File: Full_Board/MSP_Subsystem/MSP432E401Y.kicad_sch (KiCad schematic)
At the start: 4 parts, among them J1-J3 Conn_01x10, J4-J2 Conn_01x10, J5-J7 Conn_01x10, J8-J6 Conn_01x10

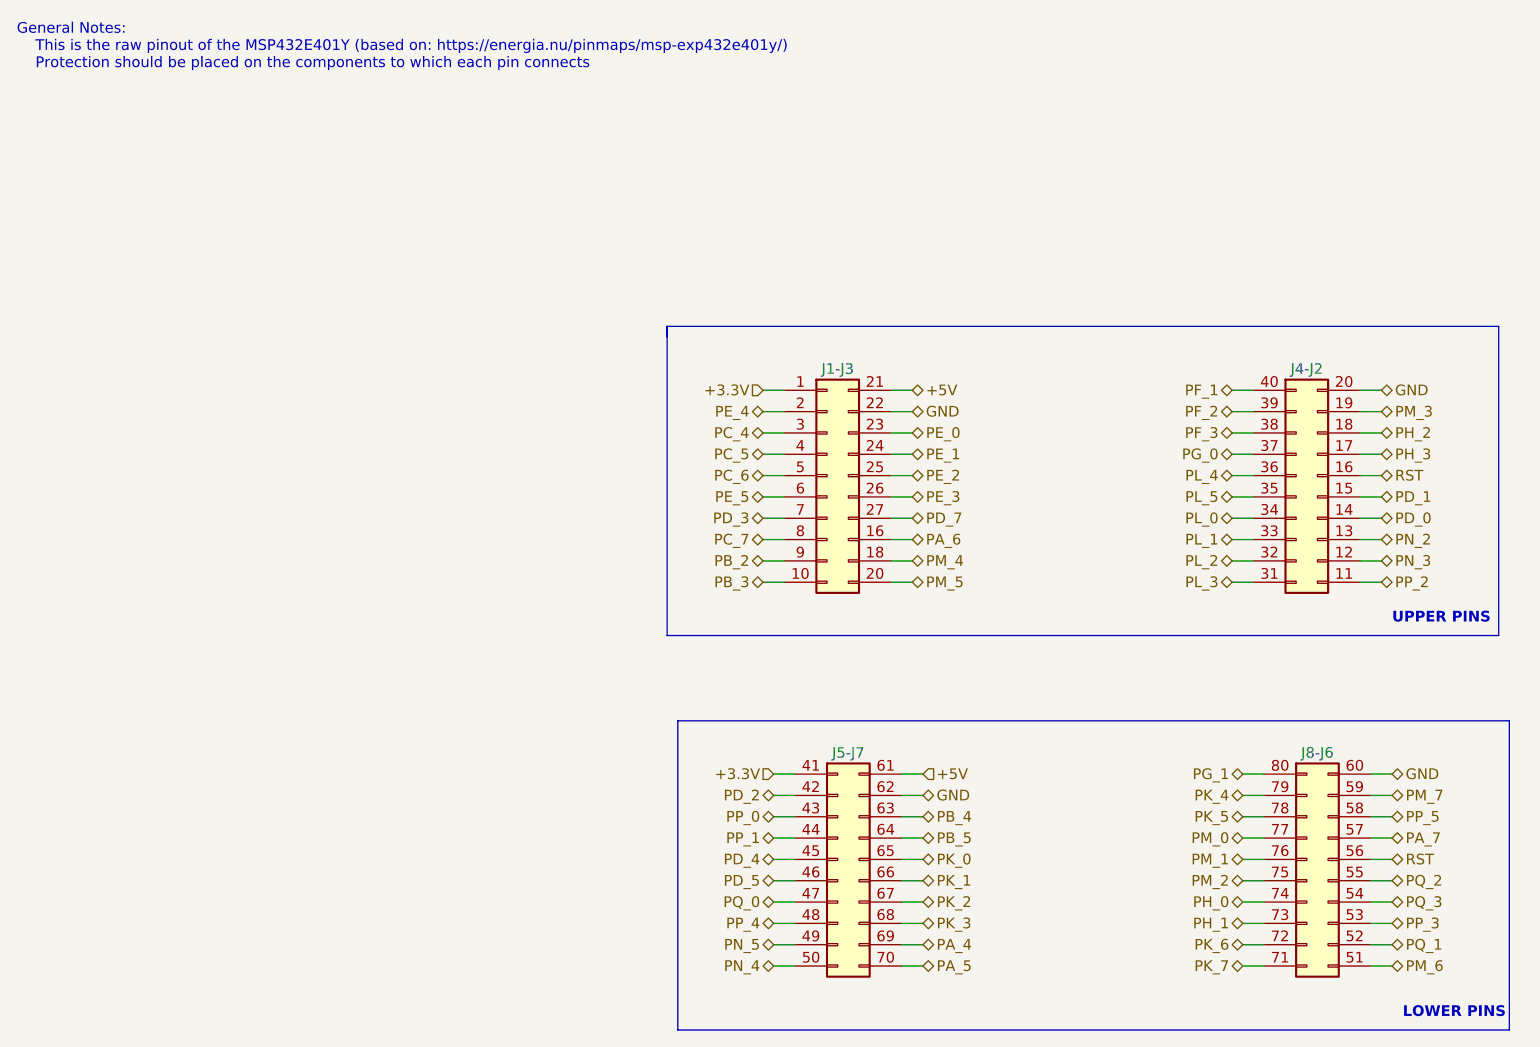
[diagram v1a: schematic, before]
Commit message: Add digikey/mouser components to stepper and button subsystems
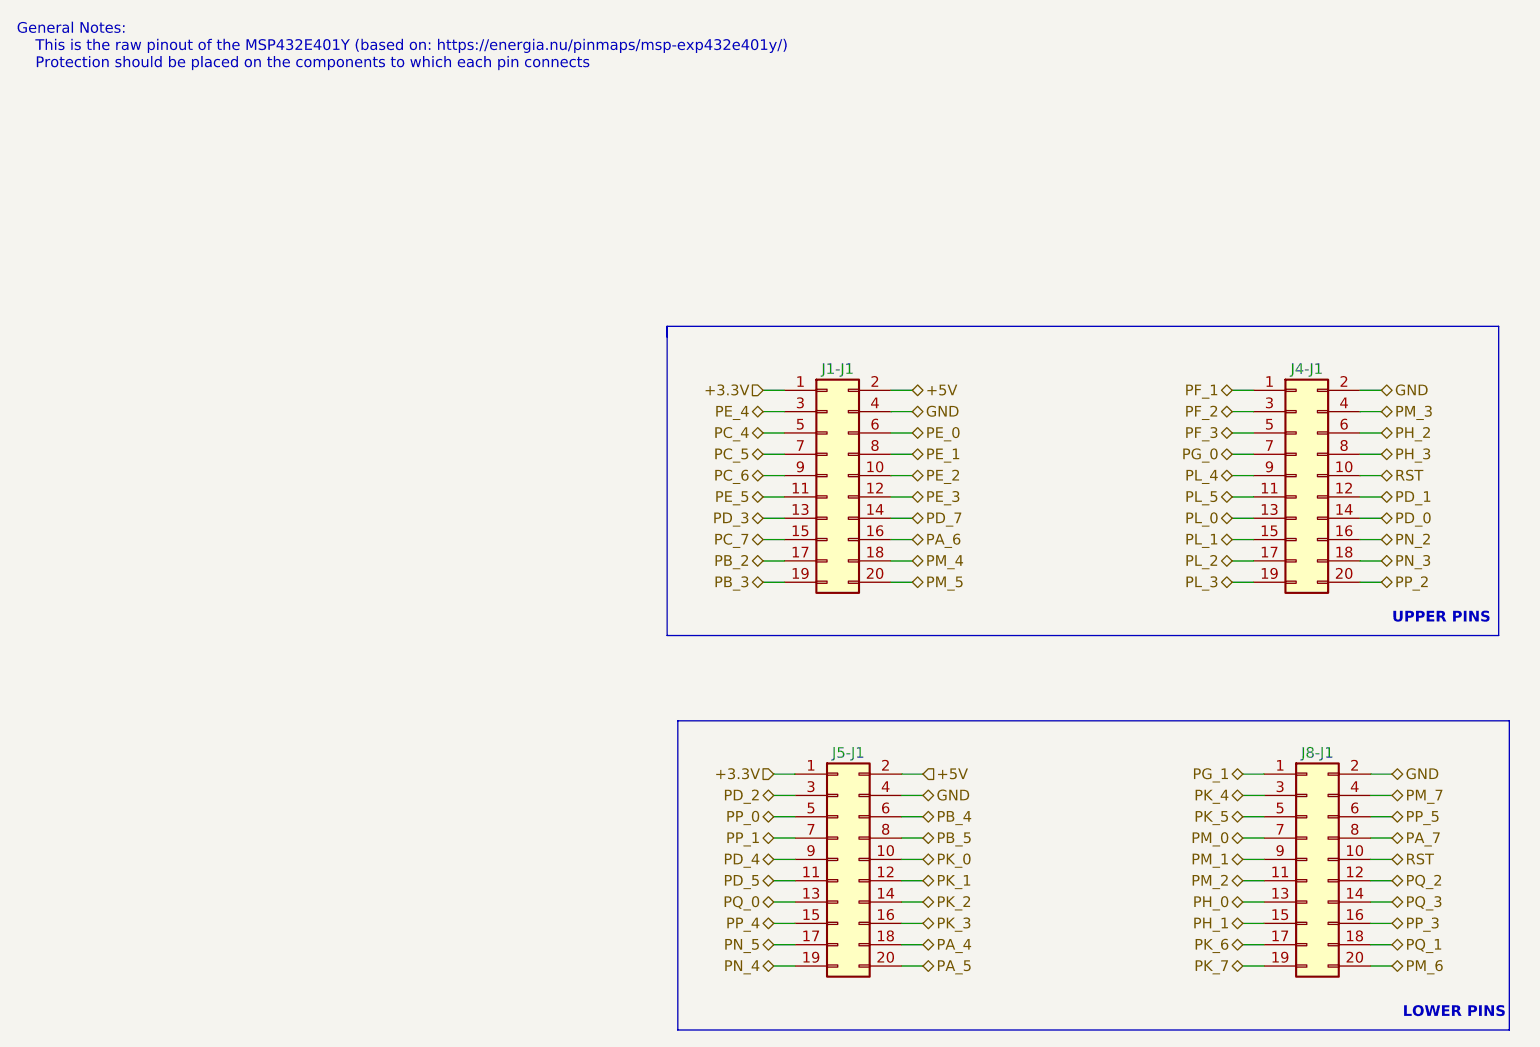
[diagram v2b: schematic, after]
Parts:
- renumbered J1-J3 to J1-J1, J4-J2 to J4-J1, J5-J7 to J5-J1, J8-J6 to J8-J1
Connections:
- net +3.3V: now also J5-J1.1 (Pin_1); no longer J5-J1.41 (Pin_41)
- net +5V: now also J1-J1.2 (Pin_2), J5-J1.2 (Pin_2); no longer J1-J1.21 (Pin_21), J5-J1.61 (Pin_61)
- net GND: now also J1-J1.4 (Pin_4), J4-J1.2 (Pin_2), J5-J1.4 (Pin_4), J8-J1.2 (Pin_2); no longer J1-J1.22 (Pin_22), J4-J1.20 (Pin_20), J5-J1.62 (Pin_62), J8-J1.60 (Pin_60)
- net PA_4: now also J5-J1.18 (Pin_18); no longer J5-J1.69 (Pin_69)
- net PA_5: now also J5-J1.20 (Pin_20); no longer J5-J1.70 (Pin_70)
- net PA_7: now also J8-J1.8 (Pin_8); no longer J8-J1.57 (Pin_57)
- net PB_2: now also J1-J1.17 (Pin_17); no longer J1-J1.9 (Pin_9)
- net PB_3: now also J1-J1.19 (Pin_19); no longer J1-J1.10 (Pin_10)
- net PB_4: now also J5-J1.6 (Pin_6); no longer J5-J1.63 (Pin_63)
- net PB_5: now also J5-J1.8 (Pin_8); no longer J5-J1.64 (Pin_64)
- net PC_4: now also J1-J1.5 (Pin_5); no longer J1-J1.3 (Pin_3)
- net PC_5: now also J1-J1.7 (Pin_7); no longer J1-J1.4
- net PC_6: now also J1-J1.9 (Pin_9); no longer J1-J1.5 (Pin_5)
- net PC_7: now also J1-J1.15 (Pin_15); no longer J1-J1.8 (Pin_8)
- net PD_1: now also J4-J1.12 (Pin_12); no longer J4-J1.15 (Pin_15)
- net PD_2: now also J5-J1.3 (Pin_3); no longer J5-J1.42 (Pin_42)
- net PD_3: now also J1-J1.13 (Pin_13); no longer J1-J1.7 (Pin_7)
- net PD_4: now also J5-J1.9 (Pin_9); no longer J5-J1.45 (Pin_45)
- net PD_5: now also J5-J1.11 (Pin_11); no longer J5-J1.46 (Pin_46)
- net PD_7: now also J1-J1.14 (Pin_14); no longer J1-J1.27 (Pin_27)
- net PE_0: now also J1-J1.6 (Pin_6); no longer J1-J1.23 (Pin_23)
- net PE_1: now also J1-J1.8 (Pin_8); no longer J1-J1.24 (Pin_24)
- net PE_2: now also J1-J1.10 (Pin_10); no longer J1-J1.25 (Pin_25)
- net PE_3: now also J1-J1.12 (Pin_12); no longer J1-J1.26 (Pin_26)
- net PE_4: now also J1-J1.3 (Pin_3); no longer J1-J1.2 (Pin_2)
- net PE_5: now also J1-J1.11 (Pin_11); no longer J1-J1.6 (Pin_6)
- net PF_1: now also J4-J1.1 (Pin_1); no longer J4-J1.40 (Pin_40)
- net PF_2: now also J4-J1.3 (Pin_3); no longer J4-J1.39 (Pin_39)
- net PF_3: now also J4-J1.5 (Pin_5); no longer J4-J1.38 (Pin_38)
- net PG_0: now also J4-J1.7 (Pin_7); no longer J4-J1.37 (Pin_37)
- net PG_1: now also J8-J1.1 (Pin_1); no longer J8-J1.80 (Pin_80)
- net PH_0: now also J8-J1.13 (Pin_13); no longer J8-J1.74 (Pin_74)
- net PH_1: now also J8-J1.15 (Pin_15); no longer J8-J1.73 (Pin_73)
- net PH_2: now also J4-J1.6 (Pin_6); no longer J4-J1.18 (Pin_18)
- net PH_3: now also J4-J1.8 (Pin_8); no longer J4-J1.17 (Pin_17)
- net PK_0: now also J5-J1.10 (Pin_10); no longer J5-J1.65 (Pin_65)
- net PK_1: now also J5-J1.12 (Pin_12); no longer J5-J1.66 (Pin_66)
- net PK_2: now also J5-J1.14 (Pin_14); no longer J5-J1.67 (Pin_67)
- net PK_3: now also J5-J1.16 (Pin_16); no longer J5-J1.68 (Pin_68)
- net PK_4: now also J8-J1.3 (Pin_3); no longer J8-J1.79 (Pin_79)
- net PK_5: now also J8-J1.5 (Pin_5); no longer J8-J1.78 (Pin_78)
- net PK_6: now also J8-J1.17 (Pin_17); no longer J8-J1.72 (Pin_72)
- net PK_7: now also J8-J1.19 (Pin_19); no longer J8-J1.71 (Pin_71)
- net PL_0: now also J4-J1.13 (Pin_13); no longer J4-J1.34 (Pin_34)
- net PL_1: now also J4-J1.15 (Pin_15); no longer J4-J1.33 (Pin_33)
- net PL_2: now also J4-J1.17 (Pin_17); no longer J4-J1.32 (Pin_32)
- net PL_3: now also J4-J1.19 (Pin_19); no longer J4-J1.31 (Pin_31)
- net PL_4: now also J4-J1.9 (Pin_9); no longer J4-J1.36 (Pin_36)
- net PL_5: now also J4-J1.11 (Pin_11); no longer J4-J1.35 (Pin_35)
- net PM_0: now also J8-J1.7 (Pin_7); no longer J8-J1.77 (Pin_77)
- net PM_1: now also J8-J1.9 (Pin_9); no longer J8-J1.76 (Pin_76)
- net PM_2: now also J8-J1.11 (Pin_11); no longer J8-J1.75 (Pin_75)
- net PM_3: now also J4-J1.4 (Pin_4); no longer J4-J1.19 (Pin_19)
- net PM_6: now also J8-J1.20 (Pin_20); no longer J8-J1.51 (Pin_51)
- net PM_7: now also J8-J1.4 (Pin_4); no longer J8-J1.59 (Pin_59)
- net PN_2: now also J4-J1.16 (Pin_16); no longer J4-J1.13 (Pin_13)
- net PN_3: now also J4-J1.18 (Pin_18); no longer J4-J1.12 (Pin_12)
- net PN_4: now also J5-J1.19 (Pin_19); no longer J5-J1.50 (Pin_50)
- net PN_5: now also J5-J1.17 (Pin_17); no longer J5-J1.49 (Pin_49)
- net PP_0: now also J5-J1.5 (Pin_5); no longer J5-J1.43 (Pin_43)
- net PP_1: now also J5-J1.7 (Pin_7); no longer J5-J1.44 (Pin_44)
- net PP_2: now also J4-J1.20 (Pin_20); no longer J4-J1.11 (Pin_11)
- net PP_3: now also J8-J1.16 (Pin_16); no longer J8-J1.53 (Pin_53)
- net PP_4: now also J5-J1.15 (Pin_15); no longer J5-J1.48 (Pin_48)
- net PP_5: now also J8-J1.6 (Pin_6); no longer J8-J1.58 (Pin_58)
- net PQ_0: now also J5-J1.13 (Pin_13); no longer J5-J1.47 (Pin_47)
- net PQ_1: now also J8-J1.18 (Pin_18); no longer J8-J1.52 (Pin_52)
- net PQ_2: now also J8-J1.12 (Pin_12); no longer J8-J1.55 (Pin_55)
- net PQ_3: now also J8-J1.14 (Pin_14); no longer J8-J1.54 (Pin_54)
- net RST: now also J4-J1.10 (Pin_10), J8-J1.10 (Pin_10); no longer J4-J1.16 (Pin_16), J8-J1.56 (Pin_56)
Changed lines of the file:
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@@
     (effects (font (size 1.27 1.27)) (justify right))
   )
-  (symbol (lib_name "Conn_02x10_Odd_Even_2") (lib_id "Connector_Generic:Conn_02x10_Odd_Even") (at 167.64 71.12 0) (unit 1)
+  (symbol (lib_id "Connector_Generic:Conn_02x10_Odd_Even") (at 167.64 71.12 0) (unit 1)
     (in_bom yes) (on_board yes)
-    (property "Reference" "J4-J2" (id 0) (at 168.91 58.42 0))
+    (property "Reference" "J4-J1" (id 0) (at 168.91 58.42 0))
     (property "Value" "Conn_01x10" (id 1) (at 165.1 87.63 0)
       (effects (font (size 1.27 1.27)) hide)
@@
       (effects (font (size 1.27 1.27)) hide)
     )
+    (pin "1")
+    (pin "10")
     (pin "11")
     (pin "12")
@@
     (pin "18")
     (pin "19")
+    (pin "2")
     (pin "20")
-    (pin "31")
-    (pin "32")
-    (pin "33")
-    (pin "34")
-    (pin "35")
-    (pin "36")
-    (pin "37")
-    (pin "38")
-    (pin "39")
-    (pin "40")
+    (pin "3")
+    (pin "4")
+    (pin "5")
+    (pin "6")
+    (pin "7")
+    (pin "8")
+    (pin "9")
   )
-  (symbol (lib_name "Conn_02x10_Odd_Even_3") (lib_id "Connector_Generic:Conn_02x10_Odd_Even") (at 113.03 116.84 0) (unit 1)
+  (symbol (lib_id "Connector_Generic:Conn_02x10_Odd_Even") (at 113.03 116.84 0) (unit 1)
     (in_bom yes) (on_board yes)
-    (property "Reference" "J5-J7" (id 0) (at 114.3 104.14 0))
+    (property "Reference" "J5-J1" (id 0) (at 114.3 104.14 0))
     (property "Value" "Conn_01x10" (id 1) (at 115.57 120.65 0)
       (effects (font (size 1.27 1.27)) (justify left) hide)
@@
       (effects (font (size 1.27 1.27)) hide)
     )
-    (pin "41")
-    (pin "42")
-    (pin "43")
-    (pin "44")
-    (pin "45")
-    (pin "46")
-    (pin "47")
-    (pin "48")
-    (pin "49")
-    (pin "50")
-    (pin "61")
-    (pin "62")
-    (pin "63")
-    (pin "64")
-    (pin "65")
-    (pin "66")
-    (pin "67")
-    (pin "68")
-    (pin "69")
-    (pin "70")
+    (pin "1")
+    (pin "10")
+    (pin "11")
+    (pin "12")
+    (pin "13")
+    (pin "14")
+    (pin "15")
+    (pin "16")
+    (pin "17")
+    (pin "18")
+    (pin "19")
+    (pin "2")
+    (pin "20")
+    (pin "3")
+    (pin "4")
+    (pin "5")
+    (pin "6")
+    (pin "7")
+    (pin "8")
+    (pin "9")
   )
-  (symbol (lib_name "Conn_02x10_Odd_Even_4") (lib_id "Connector_Generic:Conn_02x10_Odd_Even") (at 168.91 116.84 0) (unit 1)
+  (symbol (lib_id "Connector_Generic:Conn_02x10_Odd_Even") (at 168.91 116.84 0) (unit 1)
     (in_bom yes) (on_board yes)
-    (property "Reference" "J8-J6" (id 0) (at 170.18 104.14 0))
+    (property "Reference" "J8-J1" (id 0) (at 170.18 104.14 0))
     (property "Value" "Conn_01x10" (id 1) (at 166.37 133.35 0)
       (effects (font (size 1.27 1.27)) hide)
@@
       (effects (font (size 1.27 1.27)) hide)
     )
-    (pin "51")
-    (pin "52")
-    (pin "53")
-    (pin "54")
-    (pin "55")
-    (pin "56")
-    (pin "57")
-    (pin "58")
-    (pin "59")
-    (pin "60")
-    (pin "71")
-    (pin "72")
-    (pin "73")
-    (pin "74")
-    (pin "75")
-    (pin "76")
-    (pin "77")
-    (pin "78")
-    (pin "79")
-    (pin "80")
+    (pin "1")
+    (pin "10")
+    (pin "11")
+    (pin "12")
+    (pin "13")
+    (pin "14")
+    (pin "15")
+    (pin "16")
+    (pin "17")
+    (pin "18")
+    (pin "19")
+    (pin "2")
+    (pin "20")
+    (pin "3")
+    (pin "4")
+    (pin "5")
+    (pin "6")
+    (pin "7")
+    (pin "8")
+    (pin "9")
   )
-  (symbol (lib_name "Conn_02x10_Odd_Even_1") (lib_id "Connector_Generic:Conn_02x10_Odd_Even") (at 111.76 71.12 0) (unit 1)
+  (symbol (lib_id "Connector_Generic:Conn_02x10_Odd_Even") (at 111.76 71.12 0) (unit 1)
     (in_bom yes) (on_board yes)
-    (property "Reference" "J1-J3" (id 0) (at 113.03 58.42 0))
+    (property "Reference" "J1-J1" (id 0) (at 113.03 58.42 0))
     (property "Value" "Conn_01x10" (id 1) (at 114.3 74.93 0)
       (effects (font (size 1.27 1.27)) (justify left) hide)
@@
     (pin "1")
     (pin "10")
+    (pin "11")
+    (pin "12")
+    (pin "13")
+    (pin "14")
+    (pin "15")
     (pin "16")
+    (pin "17")
     (pin "18")
+    (pin "19")
     (pin "2")
     (pin "20")
-    (pin "21")
-    (pin "22")
-    (pin "23")
-    (pin "24")
-    (pin "25")
-    (pin "26")
-    (pin "27")
     (pin "3")
     (pin "4")

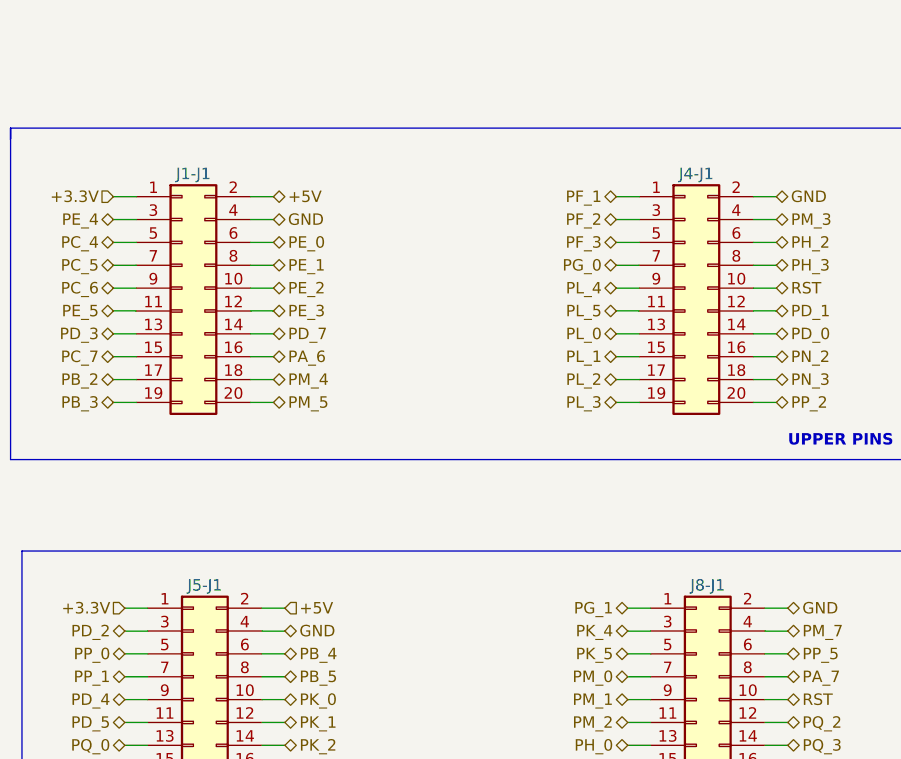
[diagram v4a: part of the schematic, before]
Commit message: Fix MSP connector spacing
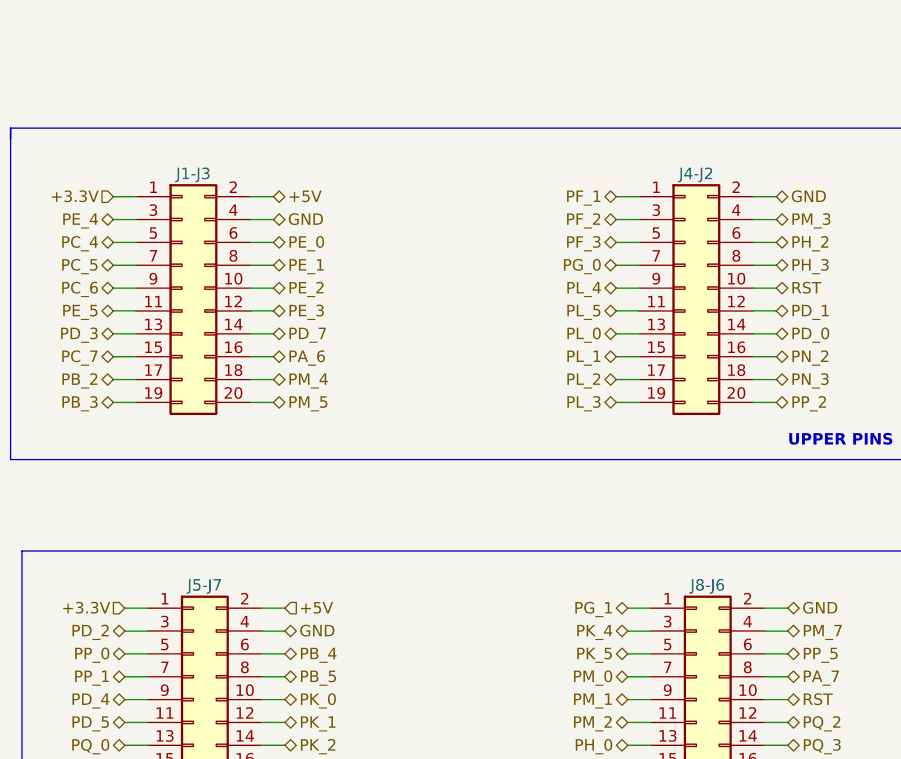
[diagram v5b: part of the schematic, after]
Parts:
- renumbered J1-J1 to J1-J3, J4-J1 to J4-J2, J5-J1 to J5-J7, J8-J1 to J8-J6
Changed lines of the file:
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@@
   (symbol (lib_id "Connector_Generic:Conn_02x10_Odd_Even") (at 167.64 71.12 0) (unit 1)
     (in_bom yes) (on_board yes)
-    (property "Reference" "J4-J1" (id 0) (at 168.91 58.42 0))
+    (property "Reference" "J4-J2" (id 0) (at 168.91 58.42 0))
     (property "Value" "Conn_01x10" (id 1) (at 165.1 87.63 0)
       (effects (font (size 1.27 1.27)) hide)
@@
   (symbol (lib_id "Connector_Generic:Conn_02x10_Odd_Even") (at 113.03 116.84 0) (unit 1)
     (in_bom yes) (on_board yes)
-    (property "Reference" "J5-J1" (id 0) (at 114.3 104.14 0))
+    (property "Reference" "J5-J7" (id 0) (at 114.3 104.14 0))
     (property "Value" "Conn_01x10" (id 1) (at 115.57 120.65 0)
       (effects (font (size 1.27 1.27)) (justify left) hide)
@@
   (symbol (lib_id "Connector_Generic:Conn_02x10_Odd_Even") (at 168.91 116.84 0) (unit 1)
     (in_bom yes) (on_board yes)
-    (property "Reference" "J8-J1" (id 0) (at 170.18 104.14 0))
+    (property "Reference" "J8-J6" (id 0) (at 170.18 104.14 0))
     (property "Value" "Conn_01x10" (id 1) (at 166.37 133.35 0)
       (effects (font (size 1.27 1.27)) hide)
@@
   (symbol (lib_id "Connector_Generic:Conn_02x10_Odd_Even") (at 111.76 71.12 0) (unit 1)
     (in_bom yes) (on_board yes)
-    (property "Reference" "J1-J1" (id 0) (at 113.03 58.42 0))
+    (property "Reference" "J1-J3" (id 0) (at 113.03 58.42 0))
     (property "Value" "Conn_01x10" (id 1) (at 114.3 74.93 0)
       (effects (font (size 1.27 1.27)) (justify left) hide)
